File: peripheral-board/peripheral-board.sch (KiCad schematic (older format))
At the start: 18 parts, among them P1001 Peripheral Bus, P1002 Power, SW1001 Power, U1001 ATTINY48-A, U1002 L78L33ACUTR

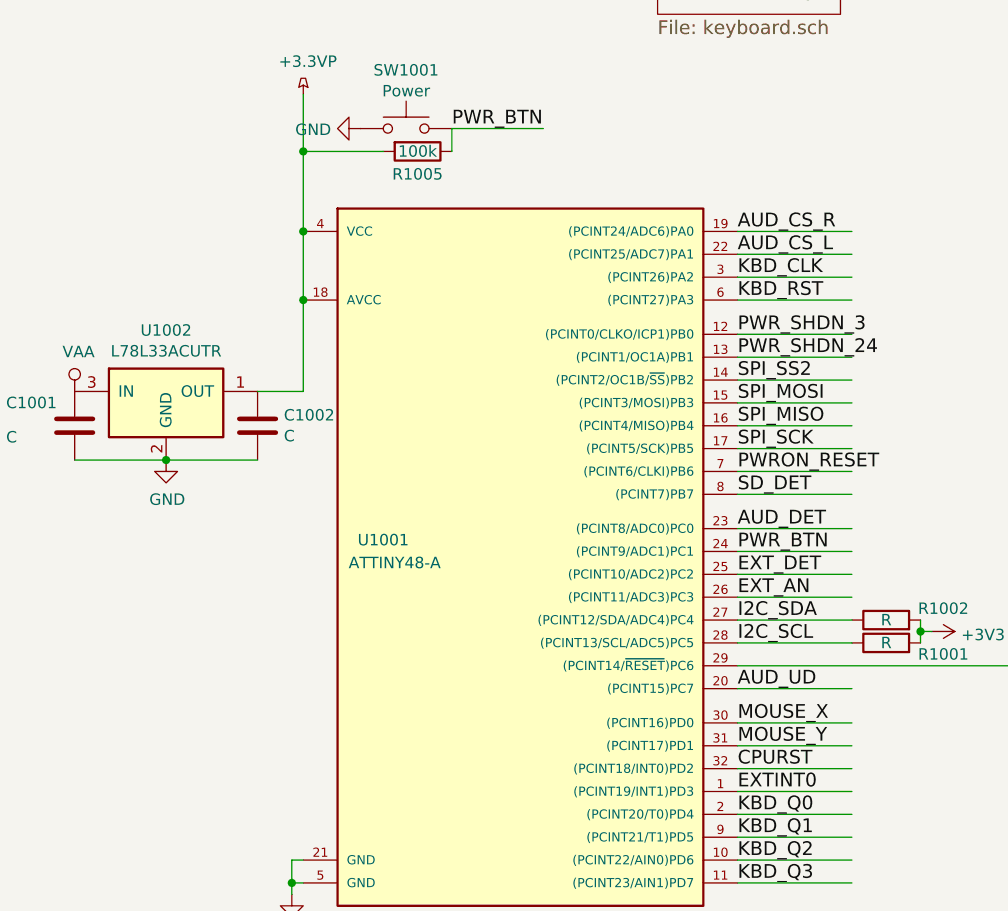
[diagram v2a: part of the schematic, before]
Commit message: routed misc signals to micro
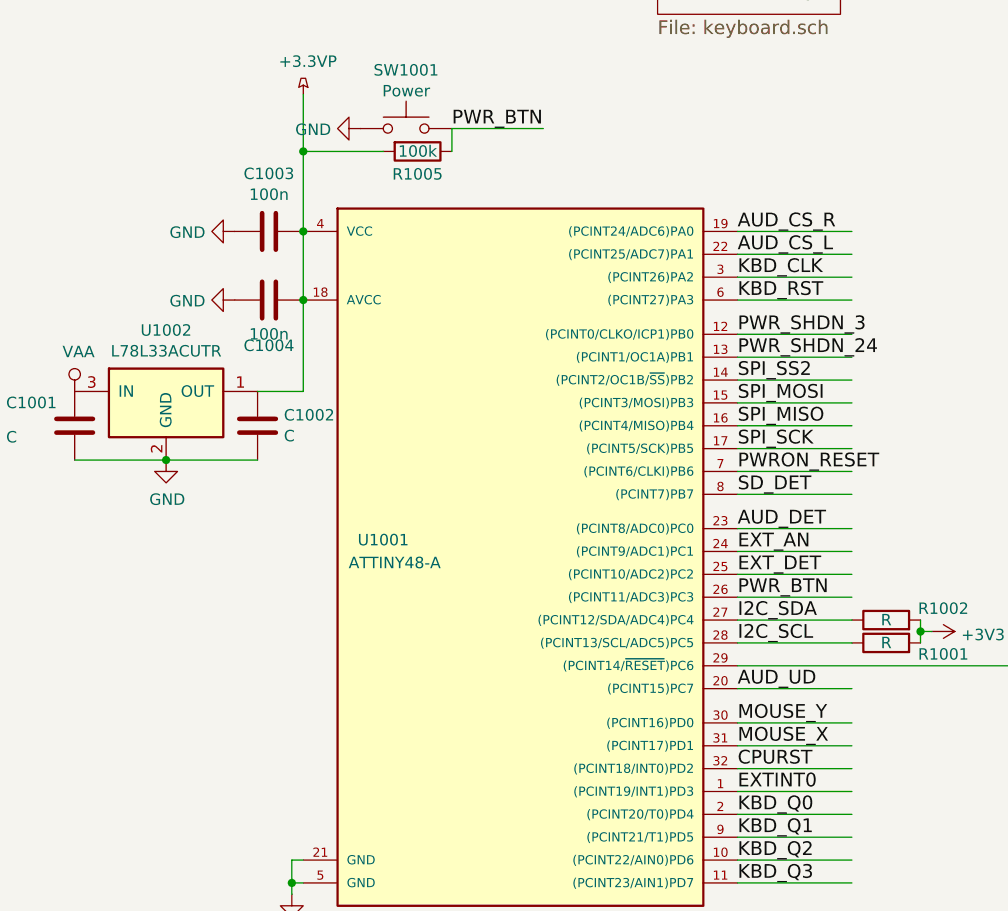
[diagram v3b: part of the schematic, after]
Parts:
- added C1003, C1004: 100n, Capacitors_SMD:C_0805, symbol C
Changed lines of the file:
@@
 Text Label 4950 4600 0    60   ~ 0
 I2C_SCL
+Text Label 4950 5050 0    60   ~ 0
+MOUSE_X
 Text Label 4950 4950 0    60   ~ 0
-MOUSE_X
-Text Label 4950 5050 0    60   ~ 0
 MOUSE_Y
 $Sheet
@@
 $EndSheet
 $Comp
-L GND #PWR01
+L GND #PWR1022
 U 1 1 581F524B
 P 3000 5700
-F 0 "#PWR01" H 3000 5450 50  0001 C CNN
+F 0 "#PWR1022" H 3000 5450 50  0001 C CNN
 F 1 "GND" H 3005 5527 50  0000 C CNN
 F 2 "" H 3000 5700 50  0000 C CNN
@@
 SPI_SS7
 $Comp
-L GND #PWR02
+L GND #PWR1003
 U 1 1 581F752E
 P 1000 1950
-F 0 "#PWR02" H 1000 1700 50  0001 C CNN
+F 0 "#PWR1003" H 1000 1700 50  0001 C CNN
 F 1 "GND" V 1005 1822 50  0000 R CNN
 F 2 "" H 1000 1950 50  0000 C CNN
@@
 $EndComp
 $Comp
-L GND #PWR03
+L GND #PWR1007
 U 1 1 581F7634
 P 1000 2800
-F 0 "#PWR03" H 1000 2550 50  0001 C CNN
+F 0 "#PWR1007" H 1000 2550 50  0001 C CNN
 F 1 "GND" V 1005 2672 50  0000 R CNN
 F 2 "" H 1000 2800 50  0000 C CNN
@@
 $EndComp
 $Comp
-L GND #PWR04
+L GND #PWR1011
 U 1 1 581F76B8
 P 1000 3200
-F 0 "#PWR04" H 1000 2950 50  0001 C CNN
+F 0 "#PWR1011" H 1000 2950 50  0001 C CNN
 F 1 "GND" V 1005 3072 50  0000 R CNN
 F 2 "" H 1000 3200 50  0000 C CNN
@@
 $EndComp
 $Comp
-L GND #PWR05
+L GND #PWR1012
 U 1 1 581F7709
 P 1000 3500
-F 0 "#PWR05" H 1000 3250 50  0001 C CNN
+F 0 "#PWR1012" H 1000 3250 50  0001 C CNN
 F 1 "GND" V 1005 3372 50  0000 R CNN
 F 2 "" H 1000 3500 50  0000 C CNN
@@
 $EndComp
 $Comp
-L GND #PWR06
+L GND #PWR1015
 U 1 1 581F7744
 P 1000 4200
-F 0 "#PWR06" H 1000 3950 50  0001 C CNN
+F 0 "#PWR1015" H 1000 3950 50  0001 C CNN
 F 1 "GND" V 1005 4072 50  0000 R CNN
 F 2 "" H 1000 4200 50  0000 C CNN
@@
 $EndComp
 $Comp
-L GND #PWR07
+L GND #PWR1017
 U 1 1 581F77D7
 P 1000 4450
-F 0 "#PWR07" H 1000 4200 50  0001 C CNN
+F 0 "#PWR1017" H 1000 4200 50  0001 C CNN
 F 1 "GND" V 1005 4322 50  0000 R CNN
 F 2 "" H 1000 4450 50  0000 C CNN
@@
 $EndComp
 $Comp
-L GND #PWR08
+L GND #PWR1020
 U 1 1 581F7812
 P 1000 4950
-F 0 "#PWR08" H 1000 4700 50  0001 C CNN
+F 0 "#PWR1020" H 1000 4700 50  0001 C CNN
 F 1 "GND" V 1005 4822 50  0000 R CNN
 F 2 "" H 1000 4950 50  0000 C CNN
@@
 $EndComp
 $Comp
-L +24V #PWR09
+L +24V #PWR1019
 U 1 1 581F7F97
 P 1000 4800
-F 0 "#PWR09" H 1000 4650 50  0001 C CNN
+F 0 "#PWR1019" H 1000 4650 50  0001 C CNN
 F 1 "+24V" V 1000 4950 50  0000 L CNN
 F 2 "" H 1000 4800 50  0000 C CNN
@@
 $EndComp
 $Comp
-L +3V3 #PWR010
+L +3V3 #PWR1021
 U 1 1 581F7FED
 P 1000 5100
-F 0 "#PWR010" H 1000 4950 50  0001 C CNN
+F 0 "#PWR1021" H 1000 4950 50  0001 C CNN
 F 1 "+3V3" V 1000 5250 50  0000 L CNN
 F 2 "" H 1000 5100 50  0000 C CNN
@@
 I2C_SCL
 $Comp
-L +3V3 #PWR011
+L +3V3 #PWR1018
 U 1 1 58A469F7
 P 5800 4550
-F 0 "#PWR011" H 5850 4600 50  0001 C CNN
+F 0 "#PWR1018" H 5850 4600 50  0001 C CNN
 F 1 "+3V3" V 5815 4678 50  0000 L CNN
 F 2 "" H -500 0   50  0001 C CNN
@@
 Text Label 4950 4300 0    60   ~ 0
 EXT_DET
-Text Label 4950 4400 0    60   ~ 0
+Text Label 4950 4200 0    60   ~ 0
 EXT_AN
 Wire Wire Line
@@
 Text Label 10400 4600 0    60   ~ 0
 EXTINT1
-Text Label 4950 4200 0    60   ~ 0
+Text Label 4950 4400 0    60   ~ 0
 PWR_BTN
 Text Label 4950 3250 0    60   ~ 0
@@
 $EndComp
 $Comp
-L GND #PWR012
+L GND #PWR1002
 U 1 1 58A4D9DD
 P 3550 1350
-F 0 "#PWR012" H 250 -650 50  0001 C CNN
+F 0 "#PWR1002" H 250 -650 50  0001 C CNN
 F 1 "GND" H 3555 1177 50  0000 C CNN
 F 2 "" H 250 -400 50  0001 C CNN
@@
 $EndComp
 $Comp
-L +3V3 #PWR013
+L +3V3 #PWR1001
 U 1 1 58A4DB27
 P 3550 750
-F 0 "#PWR013" H 100 -1200 50  0001 C CNN
+F 0 "#PWR1001" H 100 -1200 50  0001 C CNN
 F 1 "+3V3" H 3565 923 50  0000 C CNN
 F 2 "" H 100 -1050 50  0001 C CNN
@@
 Connection ~ 2450 3800
 $Comp
-L GND #PWR014
+L GND #PWR1014
 U 1 1 58A610B7
 P 2450 3800
-F 0 "#PWR014" H -200 -450 50  0001 C CNN
+F 0 "#PWR1014" H -200 -450 50  0001 C CNN
 F 1 "GND" H 2455 3627 50  0000 C CNN
 F 2 "" H -200 -200 50  0001 C CNN
@@
 $EndComp
 $Comp
-L VAA #PWR015
+L VAA #PWR1013
 U 1 1 58A6141E
 P 2050 3500
-F 0 "#PWR015" H -350 200 50  0001 C CNN
+F 0 "#PWR1013" H -350 200 50  0001 C CNN
 F 1 "VAA" H 2067 3673 50  0000 C CNN
 F 2 "" H -350 350 50  0001 C CNN
@@
 	3700 2450 3700 2350
 $Comp
-L GND #PWR016
+L GND #PWR1005
 U 1 1 58A62D39
 P 3300 2350
-F 0 "#PWR016" H -950 -400 50  0001 C CNN
+F 0 "#PWR1005" H -950 -400 50  0001 C CNN
 F 1 "GND" V 3305 2222 50  0000 R CNN
 F 2 "" H -950 -150 50  0001 C CNN
@@
 	3050 2450 3400 2450
 $Comp
-L GND #PWR017
+L GND #PWR1009
 U 1 1 58A674BE
 P 8300 3050
-F 0 "#PWR017" H 8350 3100 50  0001 C CNN
+F 0 "#PWR1009" H 8350 3100 50  0001 C CNN
 F 1 "GND" H 8305 2877 50  0000 C CNN
 F 2 "" H 50  -50 50  0001 C CNN
@@
 $EndComp
 $Comp
-L +3.3VP #PWR018
+L +3.3VP #PWR1004
 U 1 1 58A5F469
 P 3050 2200
-F 0 "#PWR018" H 900 -100 50  0001 C CNN
+F 0 "#PWR1004" H 900 -100 50  0001 C CNN
 F 1 "+3.3VP" H 3070 2343 50  0000 C CNN
 F 2 "" H 750 -50 50  0001 C CNN
@@
 Connection ~ 3050 2450
 $Comp
-L +3.3VP #PWR019
+L +3.3VP #PWR1006
 U 1 1 58A5FC40
 P 8300 2350
-F 0 "#PWR019" H 6150 50  50  0001 C CNN
+F 0 "#PWR1006" H 6150 50  50  0001 C CNN
 F 1 "+3.3VP" H 8320 2493 50  0000 C CNN
 F 2 "" H 6000 100 50  0001 C CNN
@@
 Connection ~ 6300 4700
 $Comp
-L +3.3VP #PWR020
+L +3.3VP #PWR1016
 U 1 1 58A6621C
 P 6300 4400
-F 0 "#PWR020" H 4150 2100 50  0001 C CNN
+F 0 "#PWR1016" H 4150 2100 50  0001 C CNN
 F 1 "+3.3VP" H 6320 4543 50  0000 C CNN
 F 2 "" H 4000 2150 50  0001 C CNN
@@
 	3200 6500 3200 6400
 $Comp
-L +3.3VP #PWR021
+L +3.3VP #PWR1024
 U 1 1 58A69C82
 P 3450 6100
-F 0 "#PWR021" H 1300 3800 50  0001 C CNN
+F 0 "#PWR1024" H 1300 3800 50  0001 C CNN
 F 1 "+3.3VP" H 3470 6243 50  0000 C CNN
 F 2 "" H 1150 3850 50  0001 C CNN
@@
 $EndComp
 $Comp
-L +3.3VP #PWR022
+L +3.3VP #PWR1023
 U 1 1 58A6A0BF
 P 3200 6100
-F 0 "#PWR022" H 1050 3800 50  0001 C CNN
+F 0 "#PWR1023" H 1050 3800 50  0001 C CNN
 F 1 "+3.3VP" H 3220 6243 50  0000 C CNN
 F 2 "" H 900 3850 50  0001 C CNN
@@
 $EndComp
 $Comp
-L GND #PWR023
+L GND #PWR1025
 U 1 1 58A6A217
 P 3500 7000
-F 0 "#PWR023" H 3550 7050 50  0001 C CNN
+F 0 "#PWR1025" H 3550 7050 50  0001 C CNN
 F 1 "GND" H 3505 6827 50  0000 C CNN
 F 2 "" H -1650 800 50  0001 C CNN
@@
 	1    0    0    -1
 $EndComp
+$Comp
+L C C1003
+U 1 1 58A68B7C
+P 2900 2800
+F 0 "C1003" V 2648 2800 50  0000 C CNN
+F 1 "100n" V 2739 2800 50  0000 C CNN
+F 2 "Capacitors_SMD:C_0805" H 588 -50 50  0001 C CNN
+F 3 "" H 550 100 50  0001 C CNN
+	1    2900 2800
+	0    1    1    0
+$EndComp
+$Comp
+L C C1004
+U 1 1 58A68D67
+P 2900 3100
+F 0 "C1004" V 3100 3100 50  0000 C CNN
+F 1 "100n" V 3050 3100 50  0000 C CNN
+F 2 "Capacitors_SMD:C_0805" H 38  -150 50  0001 C CNN
+F 3 "" H 0   0   50  0001 C CNN
+	1    2900 3100
+	0    1    1    0
+$EndComp
+$Comp
+L GND #PWR1008
+U 1 1 58A69569
+P 2750 2800
+F 0 "#PWR1008" H 450 50  50  0001 C CNN
+F 1 "GND" V 2755 2672 50  0000 R CNN
+F 2 "" H 450 300 50  0001 C CNN
+F 3 "" H 450 300 50  0001 C CNN
+	1    2750 2800
+	0    1    1    0
+$EndComp
+$Comp
+L GND #PWR1010
+U 1 1 58A69716
+P 2750 3100
+F 0 "#PWR1010" H 50  -250 50  0001 C CNN
+F 1 "GND" V 2755 2972 50  0000 R CNN
+F 2 "" H 50  0   50  0001 C CNN
+F 3 "" H 50  0   50  0001 C CNN
+	1    2750 3100
+	0    1    1    0
+$EndComp
 $EndSCHEMATC

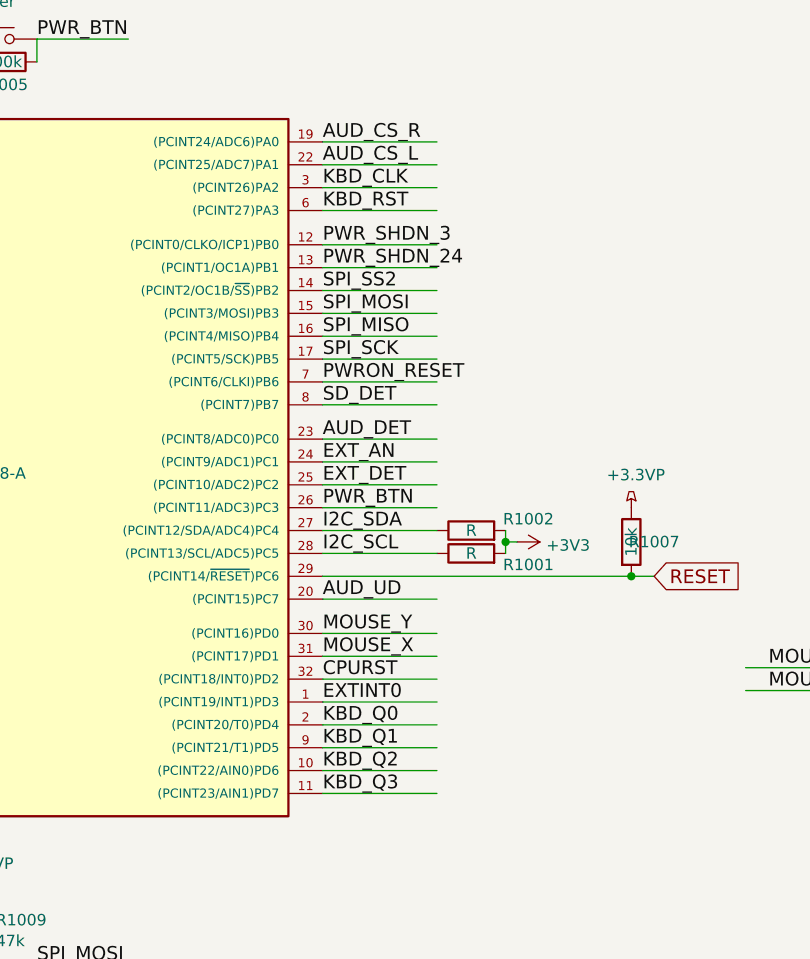
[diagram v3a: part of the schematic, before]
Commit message: misc traces, headphone jack 3d
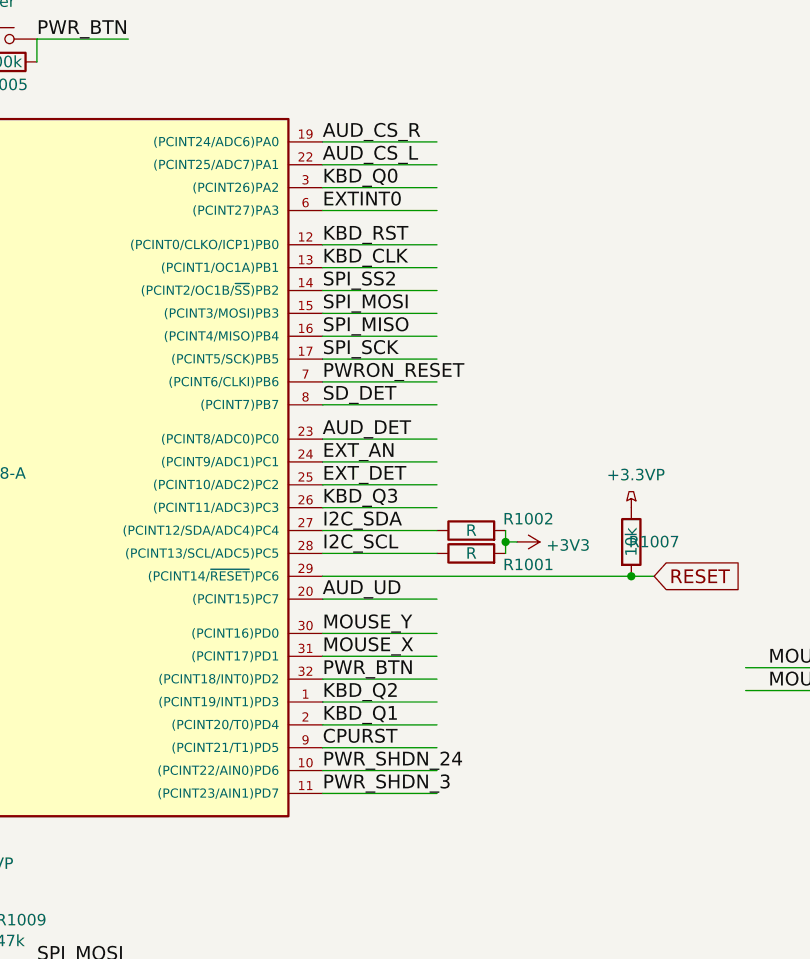
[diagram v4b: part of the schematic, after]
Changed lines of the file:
@@
 $EndSheet
 $Comp
-L GND #PWR1022
+L GND #PWR01
 U 1 1 581F524B
 P 3000 5700
-F 0 "#PWR1022" H 3000 5450 50  0001 C CNN
+F 0 "#PWR01" H 3000 5450 50  0001 C CNN
 F 1 "GND" H 3005 5527 50  0000 C CNN
 F 2 "" H 3000 5700 50  0000 C CNN
@@
 SPI_SS7
 $Comp
-L GND #PWR1003
+L GND #PWR02
 U 1 1 581F752E
 P 1000 1950
-F 0 "#PWR1003" H 1000 1700 50  0001 C CNN
+F 0 "#PWR02" H 1000 1700 50  0001 C CNN
 F 1 "GND" V 1005 1822 50  0000 R CNN
 F 2 "" H 1000 1950 50  0000 C CNN
@@
 $EndComp
 $Comp
-L GND #PWR1007
+L GND #PWR03
 U 1 1 581F7634
 P 1000 2800
-F 0 "#PWR1007" H 1000 2550 50  0001 C CNN
+F 0 "#PWR03" H 1000 2550 50  0001 C CNN
 F 1 "GND" V 1005 2672 50  0000 R CNN
 F 2 "" H 1000 2800 50  0000 C CNN
@@
 $EndComp
 $Comp
-L GND #PWR1011
+L GND #PWR04
 U 1 1 581F76B8
 P 1000 3200
-F 0 "#PWR1011" H 1000 2950 50  0001 C CNN
+F 0 "#PWR04" H 1000 2950 50  0001 C CNN
 F 1 "GND" V 1005 3072 50  0000 R CNN
 F 2 "" H 1000 3200 50  0000 C CNN
@@
 $EndComp
 $Comp
-L GND #PWR1012
+L GND #PWR05
 U 1 1 581F7709
 P 1000 3500
-F 0 "#PWR1012" H 1000 3250 50  0001 C CNN
+F 0 "#PWR05" H 1000 3250 50  0001 C CNN
 F 1 "GND" V 1005 3372 50  0000 R CNN
 F 2 "" H 1000 3500 50  0000 C CNN
@@
 $EndComp
 $Comp
-L GND #PWR1015
+L GND #PWR06
 U 1 1 581F7744
 P 1000 4200
-F 0 "#PWR1015" H 1000 3950 50  0001 C CNN
+F 0 "#PWR06" H 1000 3950 50  0001 C CNN
 F 1 "GND" V 1005 4072 50  0000 R CNN
 F 2 "" H 1000 4200 50  0000 C CNN
@@
 $EndComp
 $Comp
-L GND #PWR1017
+L GND #PWR07
 U 1 1 581F77D7
 P 1000 4450
-F 0 "#PWR1017" H 1000 4200 50  0001 C CNN
+F 0 "#PWR07" H 1000 4200 50  0001 C CNN
 F 1 "GND" V 1005 4322 50  0000 R CNN
 F 2 "" H 1000 4450 50  0000 C CNN
@@
 $EndComp
 $Comp
-L GND #PWR1020
+L GND #PWR08
 U 1 1 581F7812
 P 1000 4950
-F 0 "#PWR1020" H 1000 4700 50  0001 C CNN
+F 0 "#PWR08" H 1000 4700 50  0001 C CNN
 F 1 "GND" V 1005 4822 50  0000 R CNN
 F 2 "" H 1000 4950 50  0000 C CNN
@@
 $EndComp
 $Comp
-L +24V #PWR1019
+L +24V #PWR09
 U 1 1 581F7F97
 P 1000 4800
-F 0 "#PWR1019" H 1000 4650 50  0001 C CNN
+F 0 "#PWR09" H 1000 4650 50  0001 C CNN
 F 1 "+24V" V 1000 4950 50  0000 L CNN
 F 2 "" H 1000 4800 50  0000 C CNN
@@
 $EndComp
 $Comp
-L +3V3 #PWR1021
+L +3V3 #PWR010
 U 1 1 581F7FED
 P 1000 5100
-F 0 "#PWR1021" H 1000 4950 50  0001 C CNN
+F 0 "#PWR010" H 1000 4950 50  0001 C CNN
 F 1 "+3V3" V 1000 5250 50  0000 L CNN
 F 2 "" H 1000 5100 50  0000 C CNN
@@
 I2C_SCL
 $Comp
-L +3V3 #PWR1018
+L +3V3 #PWR011
 U 1 1 58A469F7
 P 5800 4550
-F 0 "#PWR1018" H 5850 4600 50  0001 C CNN
+F 0 "#PWR011" H 5850 4600 50  0001 C CNN
 F 1 "+3V3" V 5815 4678 50  0000 L CNN
 F 2 "" H -500 0   50  0001 C CNN
@@
 	5450 4300 4950 4300
 Wire Wire Line
-	5450 4400 4950 4400
-Wire Wire Line
-	5450 3000 4950 3000
-Wire Wire Line
-	5450 3100 4950 3100
+	5450 5150 4950 5150
+Wire Wire Line
+	5450 3350 4950 3350
+Wire Wire Line
+	5450 3250 4950 3250
+Text Label 4950 3000 0    60   ~ 0
+KBD_Q0
 Text Label 4950 5350 0    60   ~ 0
-KBD_Q0
-Text Label 4950 5450 0    60   ~ 0
 KBD_Q1
-Text Label 4950 5550 0    60   ~ 0
+Text Label 4950 5250 0    60   ~ 0
 KBD_Q2
-Text Label 4950 5650 0    60   ~ 0
+Text Label 4950 4400 0    60   ~ 0
 KBD_Q3
-Text Label 4950 3000 0    60   ~ 0
+Text Label 4950 3350 0    60   ~ 0
 KBD_CLK
-Text Label 4950 3100 0    60   ~ 0
+Text Label 4950 3250 0    60   ~ 0
 KBD_RST
 Text Label 3700 2350 0    60   ~ 0
 PWR_BTN
-Text Label 4950 5250 0    60   ~ 0
+Text Label 4950 3100 0    60   ~ 0
 EXTINT0
 Text Label 10400 4600 0    60   ~ 0
 EXTINT1
-Text Label 4950 4400 0    60   ~ 0
+Text Label 4950 5150 0    60   ~ 0
 PWR_BTN
-Text Label 4950 3250 0    60   ~ 0
+Text Label 4950 5650 0    60   ~ 0
 PWR_SHDN_3
-Text Label 4950 3350 0    60   ~ 0
+Text Label 4950 5550 0    60   ~ 0
 PWR_SHDN_24
 Wire Wire Line
-	4950 3250 5450 3250
-Wire Wire Line
-	4950 3350 5450 3350
+	4950 5650 5450 5650
+Wire Wire Line
+	4950 5550 5450 5550
 Text Label 4950 3850 0    60   ~ 0
 PWRON_RESET
-Text Label 4950 5150 0    60   ~ 0
+Text Label 4950 5450 0    60   ~ 0
 CPURST
 Wire Wire Line
 	4950 3850 5450 3850
 Wire Wire Line
-	4950 5150 5450 5150
+	4950 5450 5450 5450
 NoConn ~ 1400 1800
 NoConn ~ 1400 2100
@@
 	4950 2800 5450 2800
 Wire Wire Line
+	4950 3100 5450 3100
+Wire Wire Line
+	4950 3000 5450 3000
+Wire Wire Line
+	4950 5350 5450 5350
+Wire Wire Line
 	4950 5250 5450 5250
 Wire Wire Line
-	4950 5350 5450 5350
-Wire Wire Line
-	4950 5450 5450 5450
-Wire Wire Line
-	4950 5550 5450 5550
-Wire Wire Line
-	4950 5650 5450 5650
+	4950 4400 5450 4400
 Wire Wire Line
 	4950 3950 5450 3950
@@
 $EndComp
 $Comp
-L GND #PWR1002
+L GND #PWR012
 U 1 1 58A4D9DD
 P 3550 1350
-F 0 "#PWR1002" H 250 -650 50  0001 C CNN
+F 0 "#PWR012" H 250 -650 50  0001 C CNN
 F 1 "GND" H 3555 1177 50  0000 C CNN
 F 2 "" H 250 -400 50  0001 C CNN
@@
 $EndComp
 $Comp
-L +3V3 #PWR1001
+L +3V3 #PWR013
 U 1 1 58A4DB27
 P 3550 750
-F 0 "#PWR1001" H 100 -1200 50  0001 C CNN
+F 0 "#PWR013" H 100 -1200 50  0001 C CNN
 F 1 "+3V3" H 3565 923 50  0000 C CNN
 F 2 "" H 100 -1050 50  0001 C CNN
@@
 Connection ~ 2450 3800
 $Comp
-L GND #PWR1014
+L GND #PWR014
 U 1 1 58A610B7
 P 2450 3800
-F 0 "#PWR1014" H -200 -450 50  0001 C CNN
+F 0 "#PWR014" H -200 -450 50  0001 C CNN
 F 1 "GND" H 2455 3627 50  0000 C CNN
 F 2 "" H -200 -200 50  0001 C CNN
@@
 $EndComp
 $Comp
-L VAA #PWR1013
+L VAA #PWR015
 U 1 1 58A6141E
 P 2050 3500
-F 0 "#PWR1013" H -350 200 50  0001 C CNN
+F 0 "#PWR015" H -350 200 50  0001 C CNN
 F 1 "VAA" H 2067 3673 50  0000 C CNN
 F 2 "" H -350 350 50  0001 C CNN
@@
 	3700 2450 3700 2350
 $Comp
-L GND #PWR1005
+L GND #PWR016
 U 1 1 58A62D39
 P 3300 2350
-F 0 "#PWR1005" H -950 -400 50  0001 C CNN
+F 0 "#PWR016" H -950 -400 50  0001 C CNN
 F 1 "GND" V 3305 2222 50  0000 R CNN
 F 2 "" H -950 -150 50  0001 C CNN
@@
 	3050 2450 3400 2450
 $Comp
-L GND #PWR1009
+L GND #PWR017
 U 1 1 58A674BE
 P 8300 3050
-F 0 "#PWR1009" H 8350 3100 50  0001 C CNN
+F 0 "#PWR017" H 8350 3100 50  0001 C CNN
 F 1 "GND" H 8305 2877 50  0000 C CNN
 F 2 "" H 50  -50 50  0001 C CNN
@@
 $EndComp
 $Comp
-L +3.3VP #PWR1004
+L +3.3VP #PWR018
 U 1 1 58A5F469
 P 3050 2200
-F 0 "#PWR1004" H 900 -100 50  0001 C CNN
+F 0 "#PWR018" H 900 -100 50  0001 C CNN
 F 1 "+3.3VP" H 3070 2343 50  0000 C CNN
 F 2 "" H 750 -50 50  0001 C CNN
@@
 Connection ~ 3050 2450
 $Comp
-L +3.3VP #PWR1006
+L +3.3VP #PWR019
 U 1 1 58A5FC40
 P 8300 2350
-F 0 "#PWR1006" H 6150 50  50  0001 C CNN
+F 0 "#PWR019" H 6150 50  50  0001 C CNN
 F 1 "+3.3VP" H 8320 2493 50  0000 C CNN
 F 2 "" H 6000 100 50  0001 C CNN
@@
 Connection ~ 6300 4700
 $Comp
-L +3.3VP #PWR1016
+L +3.3VP #PWR020
 U 1 1 58A6621C
 P 6300 4400
-F 0 "#PWR1016" H 4150 2100 50  0001 C CNN
+F 0 "#PWR020" H 4150 2100 50  0001 C CNN
 F 1 "+3.3VP" H 6320 4543 50  0000 C CNN
 F 2 "" H 4000 2150 50  0001 C CNN
@@
 	3200 6500 3200 6400
 $Comp
-L +3.3VP #PWR1024
+L +3.3VP #PWR021
 U 1 1 58A69C82
 P 3450 6100
-F 0 "#PWR1024" H 1300 3800 50  0001 C CNN
+F 0 "#PWR021" H 1300 3800 50  0001 C CNN
 F 1 "+3.3VP" H 3470 6243 50  0000 C CNN
 F 2 "" H 1150 3850 50  0001 C CNN
@@
 $EndComp
 $Comp
-L +3.3VP #PWR1023
+L +3.3VP #PWR022
 U 1 1 58A6A0BF
 P 3200 6100
-F 0 "#PWR1023" H 1050 3800 50  0001 C CNN
+F 0 "#PWR022" H 1050 3800 50  0001 C CNN
 F 1 "+3.3VP" H 3220 6243 50  0000 C CNN
 F 2 "" H 900 3850 50  0001 C CNN
@@
 $EndComp
 $Comp
-L GND #PWR1025
+L GND #PWR023
 U 1 1 58A6A217
 P 3500 7000
-F 0 "#PWR1025" H 3550 7050 50  0001 C CNN
+F 0 "#PWR023" H 3550 7050 50  0001 C CNN
 F 1 "GND" H 3505 6827 50  0000 C CNN
 F 2 "" H -1650 800 50  0001 C CNN
@@
 $EndComp
 $Comp
-L GND #PWR1008
+L GND #PWR024
 U 1 1 58A69569
 P 2750 2800
-F 0 "#PWR1008" H 450 50  50  0001 C CNN
+F 0 "#PWR024" H 450 50  50  0001 C CNN
 F 1 "GND" V 2755 2672 50  0000 R CNN
 F 2 "" H 450 300 50  0001 C CNN
@@
 $EndComp
 $Comp
-L GND #PWR1010
+L GND #PWR025
 U 1 1 58A69716
 P 2750 3100
-F 0 "#PWR1010" H 50  -250 50  0001 C CNN
+F 0 "#PWR025" H 50  -250 50  0001 C CNN
 F 1 "GND" V 2755 2972 50  0000 R CNN
 F 2 "" H 50  0   50  0001 C CNN
